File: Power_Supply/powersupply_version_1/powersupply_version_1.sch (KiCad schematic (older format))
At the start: 31 parts

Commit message: added to schematic
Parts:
- added C?: 100nF, symbol Device:C_Small
- added C? (x2): 12pF, symbol Device:C_Small
- added J?: Conn_01x05, symbol Connector_Generic:Conn_01x05
- added R?: 10k, symbol Device:R_Small_US
- added SW?: SW_Push, symbol Switch:SW_Push
- added U?: Atmega328P-AU, symbol powersupply_version_1:Atmega328P-AU
- added U?: TFT_LCD, symbol powersupply_version_1:TFT_LCD
- added Y?: Crystal, symbol Device:Crystal_Small
- R?: value R_Small_US -> 1k
- R?: value R_Small_US -> 5.13k
- R?: value R_Small_US -> 2.57k
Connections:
- net GND: now also U?.2 (VSS), C?.1, C?.2, C?.2, J?.5 (Pin_5), SW?.2, U?.2 (GND)
- net VCC: now reaches U?.3 (VDD)
- net VCC: now also C?.1, J?.4 (Pin_4), R?.2, SW?.1, U?.1 (VCC), U?.18 (AVCC), U?.4 (VCC), U?.6 (VCC), U?.8 (LED)
- net SDA: now reaches U?.4 (SDA)
- net SDA: now also U?.26 (PC3)
- net SCL: now reaches U?.5 (SCL)
- net SCL: now also U?.27 (PC4)
- new net: R?.1, U?.29 (PC6_(rst))
- new net: C?.2, U?.7 (PB6), Y?.2
- new net: C?.1, U?.8 (PB7), Y?.1
- new net CS: U?.3 (CS), U?.32 (PD2)
- new net DC: U?.1 (PD3), U?.5 (DC)
- new net MISO: J?.2 (Pin_2), U?.16 (PB4), U?.9 (MISO)
- new net MOSI: J?.3 (Pin_3), U?.15 (PB3), U?.6 (MOSI)
- new net Reset: U?.28 (PC5), U?.4 (reset)
- new net SCK: J?.1 (Pin_1), U?.17 (PB5), U?.7 (SCK)
- no-connect marks 4 -> 14

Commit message: pwr supply changes
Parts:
- removed C? (x12): C_Small, symbol Device:C_Small
- removed C?: 100nF, symbol Device:C_Small
- removed C? (x2): 12pF, symbol Device:C_Small
- removed D?: D_Zener, symbol Device:D_Zener_Small
- removed D?: D_Zener_Small, symbol Device:D_Zener_Small
- removed L?: L_Small, symbol Device:L_Small
- removed M? (x2): MNMOS, symbol pspice:MNMOS
- removed R? (x5): R_Small_US, symbol Device:R_Small_US
- removed R?: 10k, symbol Device:R_Small_US
- removed R?: R_small, symbol Device:R_Small_US
- removed R?: R_Small, symbol Device:R_Small_US
- removed R?: 1k, symbol Device:R_Small_US
- removed R?: 5.13k, symbol Device:R_Small_US
- removed U?: LM25118, symbol powersupply_version_1:LM25118
- removed U?: Atmega328P-AU, symbol powersupply_version_1:Atmega328P-AU
- removed Y?: Crystal, symbol Device:Crystal_Small
- added C? (x2): 0.1uF, symbol Device:C_Small
- added U?: ATSAMD10D14A-SS, Package_SO:SOIC-20W_7.5x12.8mm_P1.27mm, symbol MCU_Microchip_SAMD:ATSAMD10D14A-SS
- added U?: AP1117-15, Package_TO_SOT_SMD:SOT-223-3_TabPin2, symbol Regulator_Linear:AP1117-15
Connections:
- net labels added: +3.3V, GNDREF
- wire segments 111 -> 14
- no-connect marks 14 -> 11
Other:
- moved on the sheet: R?, U?

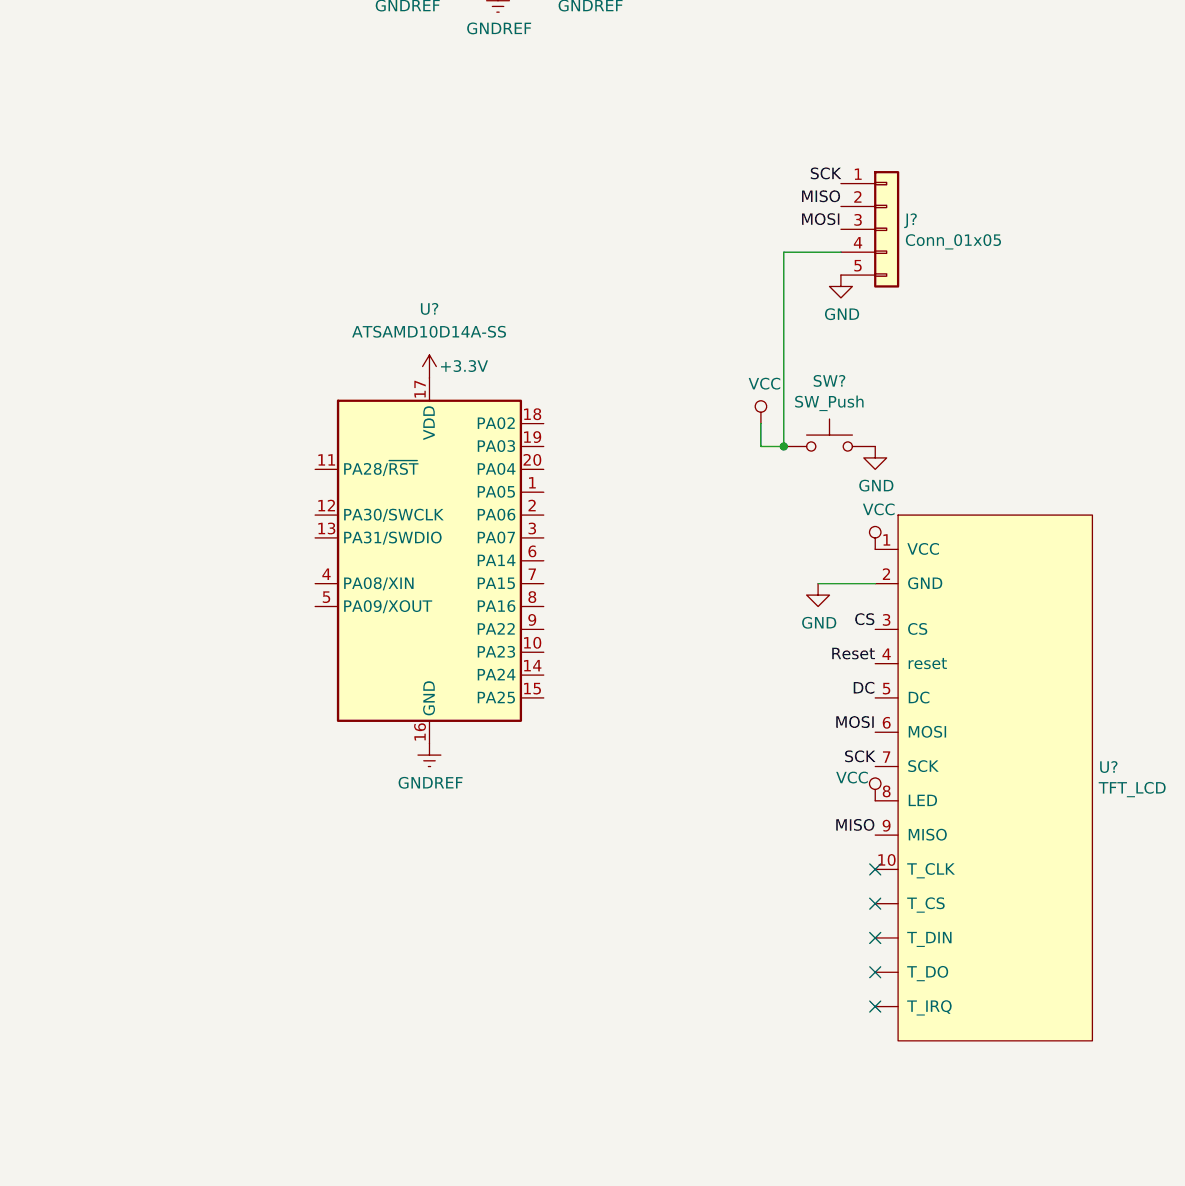
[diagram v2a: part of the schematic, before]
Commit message: removed op amp and sync connection
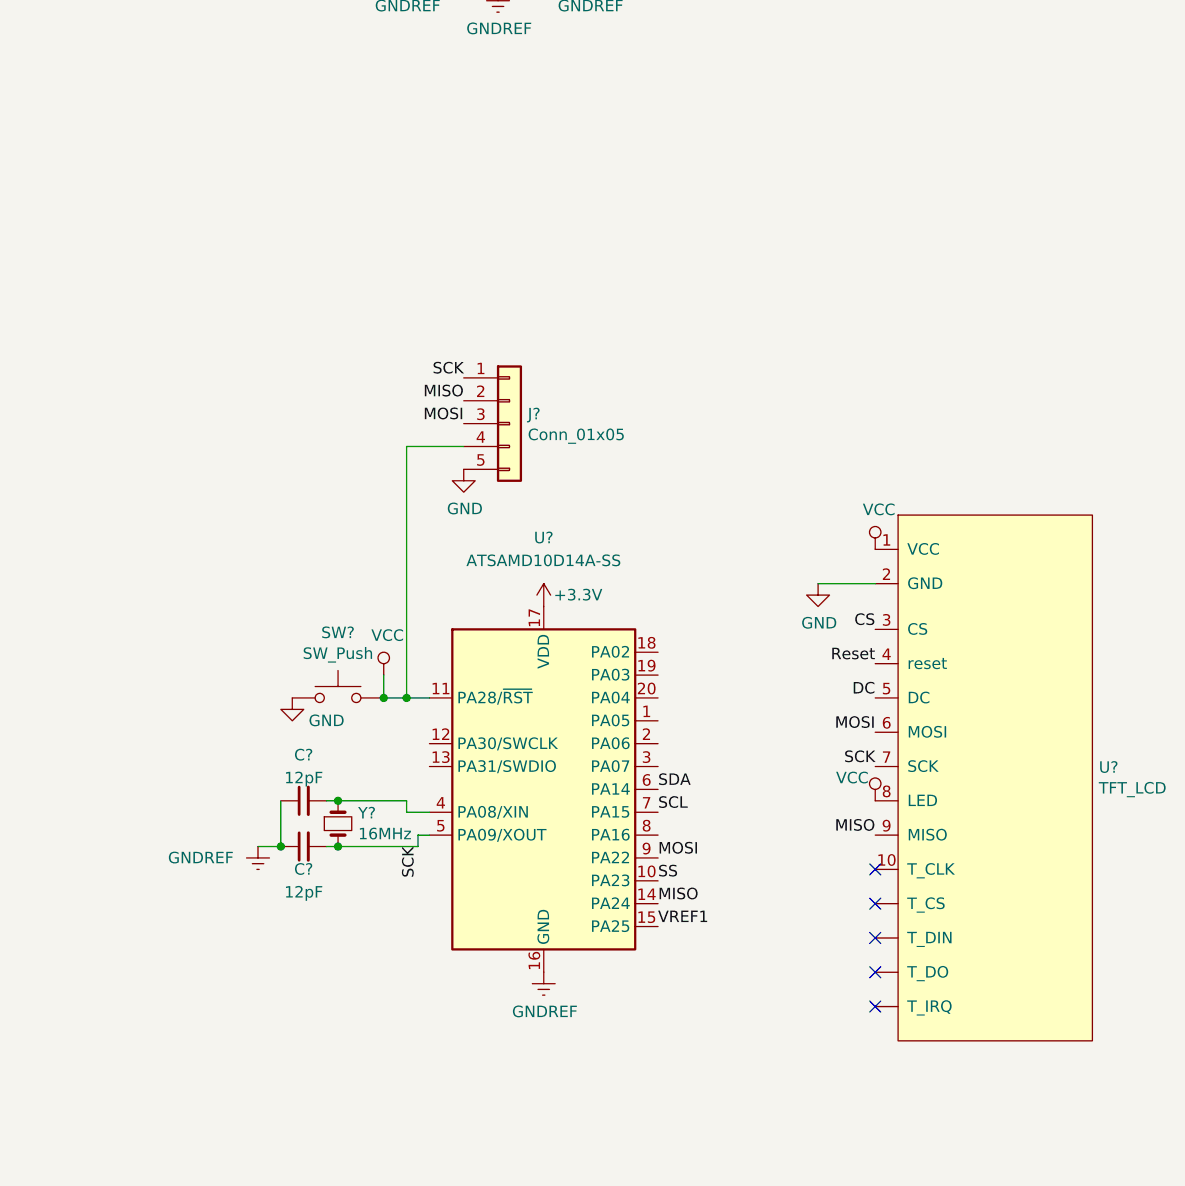
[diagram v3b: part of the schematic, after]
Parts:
- added C? (x2): 12pF, symbol Device:C_Small
- added Y?: 16MHz, symbol Device:Crystal_Small
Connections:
- net labels added: SS, VREF1
- wire segments 14 -> 25
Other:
- moved on the sheet: J?, SW?, U?
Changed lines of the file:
@@
-$Comp
-L power:VCC #PWR?
-U 1 1 5D3309E2
-P 3150 4900
-F 0 "#PWR?" H 3150 4750 50  0001 C CNN
-F 1 "VCC" H 3167 5073 50  0000 C CNN
-F 2 "" H 3150 4900 50  0001 C CNN
-F 3 "" H 3150 4900 50  0001 C CNN
-	1    3150 4900
-	1    0    0    -1
-$EndComp
-Wire Wire Line
-	3150 5000 3150 4900
-$Comp
-L Switch:SW_Push SW?
-U 1 1 5D3340CA
-P 3450 5000
-F 0 "SW?" H 3450 5285 50  0000 C CNN
-F 1 "SW_Push" H 3450 5194 50  0000 C CNN
-F 2 "" H 3450 5200 50  0001 C CNN
-F 3 "~" H 3450 5200 50  0001 C CNN
-	1    3450 5000
-	1    0    0    -1
-$EndComp
-$Comp
-L power:GND #PWR?
-U 1 1 5D335430
-P 3650 5000
-F 0 "#PWR?" H 3650 4750 50  0001 C CNN
-F 1 "GND" H 3655 4827 50  0000 C CNN
-F 2 "" H 3650 5000 50  0001 C CNN
-F 3 "" H 3650 5000 50  0001 C CNN
-	1    3650 5000
-	1    0    0    -1
-$EndComp
-Wire Wire Line
-	3150 5000 3250 5000
-Wire Wire Line
-	3250 5000 3250 4150
-Wire Wire Line
-	3250 4150 3500 4150
-Connection ~ 3250 5000
-$Comp
-L power:GND #PWR?
-U 1 1 5D33ECB0
-P 3500 4250
-F 0 "#PWR?" H 3500 4000 50  0001 C CNN
-F 1 "GND" H 3505 4077 50  0000 C CNN
-F 2 "" H 3500 4250 50  0001 C CNN
-F 3 "" H 3500 4250 50  0001 C CNN
-	1    3500 4250
-	1    0    0    -1
-$EndComp
-$Comp
-L Connector_Generic:Conn_01x05 J?
-U 1 1 5D3457C6
-P 3700 4050
-F 0 "J?" H 3780 4092 50  0000 L CNN
-F 1 "Conn_01x05" H 3780 4001 50  0000 L CNN
-F 2 "" H 3700 4050 50  0001 C CNN
-F 3 "~" H 3700 4050 50  0001 C CNN
-	1    3700 4050
-	1    0    0    -1
-$EndComp
-Text Label 3500 4050 2    50   ~ 0
-MOSI
-Text Label 3500 3950 2    50   ~ 0
-MISO
-Text Label 3500 3850 2    50   ~ 0
-SCK
 $Comp
 L power:VCC #PWR?
@@
 L MCU_Microchip_SAMD:ATSAMD10D14A-SS U?
 U 1 1 5D3D0FF3
-P 1700 5500
-F 0 "U?" H 1700 6600 50  0000 C CNN
-F 1 "ATSAMD10D14A-SS" H 1700 6500 50  0000 C CNN
-F 2 "Package_SO:SOIC-20W_7.5x12.8mm_P1.27mm" H 1700 4350 50  0001 C CNN
-F 3 "http://ww1.microchip.com/downloads/en/DeviceDoc/Atmel-42242-SAM-D10_Datasheet.pdf" H 1700 4600 50  0001 C CNN
-	1    1700 5500
+P 2200 6500
+F 0 "U?" H 2200 7600 50  0000 C CNN
+F 1 "ATSAMD10D14A-SS" H 2200 7500 50  0000 C CNN
+F 2 "Package_SO:SOIC-20W_7.5x12.8mm_P1.27mm" H 2200 5350 50  0001 C CNN
+F 3 "http://ww1.microchip.com/downloads/en/DeviceDoc/Atmel-42242-SAM-D10_Datasheet.pdf" H 2200 5600 50  0001 C CNN
+	1    2200 6500
 	1    0    0    -1
 $EndComp
@@
 L power:GNDREF #PWR?
 U 1 1 5D3FD3BC
-P 1700 6300
-F 0 "#PWR?" H 1700 6050 50  0001 C CNN
-F 1 "GNDREF" H 1705 6127 50  0000 C CNN
-F 2 "" H 1700 6300 50  0001 C CNN
-F 3 "" H 1700 6300 50  0001 C CNN
-	1    1700 6300
+P 2200 7300
+F 0 "#PWR?" H 2200 7050 50  0001 C CNN
+F 1 "GNDREF" H 2205 7127 50  0000 C CNN
+F 2 "" H 2200 7300 50  0001 C CNN
+F 3 "" H 2200 7300 50  0001 C CNN
+	1    2200 7300
 	1    0    0    -1
 $EndComp
@@
 L power:+3.3V #PWR?
 U 1 1 5D3FE02C
-P 1700 4700
-F 0 "#PWR?" H 1700 4550 50  0001 C CNN
-F 1 "+3.3V" H 1850 4750 50  0000 C CNN
-F 2 "" H 1700 4700 50  0001 C CNN
-F 3 "" H 1700 4700 50  0001 C CNN
-	1    1700 4700
-	1    0    0    -1
-$EndComp
+P 2200 5700
+F 0 "#PWR?" H 2200 5550 50  0001 C CNN
+F 1 "+3.3V" H 2350 5750 50  0000 C CNN
+F 2 "" H 2200 5700 50  0001 C CNN
+F 3 "" H 2200 5700 50  0001 C CNN
+	1    2200 5700
+	1    0    0    -1
+$EndComp
+Text Label 1850 4700 2    50   ~ 0
+SCK
+Text Label 1850 4800 2    50   ~ 0
+MISO
+Text Label 1850 4900 2    50   ~ 0
+MOSI
+$Comp
+L Connector_Generic:Conn_01x05 J?
+U 1 1 5D3457C6
+P 2050 4900
+F 0 "J?" H 2130 4942 50  0000 L CNN
+F 1 "Conn_01x05" H 2130 4851 50  0000 L CNN
+F 2 "" H 2050 4900 50  0001 C CNN
+F 3 "~" H 2050 4900 50  0001 C CNN
+	1    2050 4900
+	1    0    0    -1
+$EndComp
+$Comp
+L power:GND #PWR?
+U 1 1 5D33ECB0
+P 1850 5100
+F 0 "#PWR?" H 1850 4850 50  0001 C CNN
+F 1 "GND" H 1855 4927 50  0000 C CNN
+F 2 "" H 1850 5100 50  0001 C CNN
+F 3 "" H 1850 5100 50  0001 C CNN
+	1    1850 5100
+	1    0    0    -1
+$EndComp
+Wire Wire Line
+	1600 5000 1850 5000
+$Comp
+L power:VCC #PWR?
+U 1 1 5D3309E2
+P 1500 6000
+F 0 "#PWR?" H 1500 5850 50  0001 C CNN
+F 1 "VCC" H 1517 6173 50  0000 C CNN
+F 2 "" H 1500 6000 50  0001 C CNN
+F 3 "" H 1500 6000 50  0001 C CNN
+	1    1500 6000
+	1    0    0    -1
+$EndComp
+Wire Wire Line
+	1500 6100 1500 6000
+$Comp
+L Switch:SW_Push SW?
+U 1 1 5D3340CA
+P 1300 6100
+F 0 "SW?" H 1300 6385 50  0000 C CNN
+F 1 "SW_Push" H 1300 6294 50  0000 C CNN
+F 2 "" H 1300 6300 50  0001 C CNN
+F 3 "~" H 1300 6300 50  0001 C CNN
+	1    1300 6100
+	1    0    0    -1
+$EndComp
+$Comp
+L power:GND #PWR?
+U 1 1 5D335430
+P 1100 6100
+F 0 "#PWR?" H 1100 5850 50  0001 C CNN
+F 1 "GND" H 1250 6000 50  0000 C CNN
+F 2 "" H 1100 6100 50  0001 C CNN
+F 3 "" H 1100 6100 50  0001 C CNN
+	1    1100 6100
+	1    0    0    -1
+$EndComp
+Wire Wire Line
+	1600 5000 1600 6100
+Wire Wire Line
+	1700 6100 1600 6100
+Connection ~ 1500 6100
+Connection ~ 1600 6100
+Wire Wire Line
+	1600 6100 1500 6100
+$Comp
+L Device:Crystal_Small Y?
+U 1 1 5D41A5D2
+P 1300 6650
+F 0 "Y?" V 1254 6738 50  0000 L CNN
+F 1 "16MHz" V 1345 6738 50  0000 L CNN
+F 2 "" H 1300 6650 50  0001 C CNN
+F 3 "~" H 1300 6650 50  0001 C CNN
+	1    1300 6650
+	0    1    1    0
+$EndComp
+$Comp
+L Device:C_Small C?
+U 1 1 5D41D67B
+P 1150 6550
+F 0 "C?" V 1350 6550 50  0000 C CNN
+F 1 "12pF" V 1250 6550 50  0000 C CNN
+F 2 "" H 1150 6550 50  0001 C CNN
+F 3 "~" H 1150 6550 50  0001 C CNN
+	1    1150 6550
+	0    -1   -1   0
+$EndComp
+$Comp
+L Device:C_Small C?
+U 1 1 5D41F47A
+P 1150 6750
+F 0 "C?" V 1050 6750 50  0000 C CNN
+F 1 "12pF" V 950 6750 50  0000 C CNN
+F 2 "" H 1150 6750 50  0001 C CNN
+F 3 "~" H 1150 6750 50  0001 C CNN
+	1    1150 6750
+	0    -1   -1   0
+$EndComp
+Wire Wire Line
+	1700 6600 1600 6600
+Wire Wire Line
+	1600 6600 1600 6550
+Wire Wire Line
+	1600 6550 1300 6550
+Wire Wire Line
+	1250 6550 1300 6550
+Connection ~ 1300 6550
+Wire Wire Line
+	1300 6750 1650 6750
+Wire Wire Line
+	1650 6750 1650 6700
+Wire Wire Line
+	1650 6700 1700 6700
+$Comp
+L power:GNDREF #PWR?
+U 1 1 5D42290E
+P 950 6750
+F 0 "#PWR?" H 950 6500 50  0001 C CNN
+F 1 "GNDREF" H 700 6700 50  0000 C CNN
+F 2 "" H 950 6750 50  0001 C CNN
+F 3 "" H 950 6750 50  0001 C CNN
+	1    950  6750
+	1    0    0    -1
+$EndComp
+Wire Wire Line
+	1050 6550 1050 6750
+Wire Wire Line
+	1250 6750 1300 6750
+Connection ~ 1300 6750
+Wire Wire Line
+	950  6750 1050 6750
+Connection ~ 1050 6750
+Text Label 2700 6800 0    50   ~ 0
+MOSI
+Text Label 2700 7000 0    50   ~ 0
+MISO
+Text Label 2700 6500 0    50   ~ 0
+SDA
+Text Label 2700 6600 0    50   ~ 0
+SCL
+Text Label 1650 6750 3    50   ~ 0
+SCK
+Text Label 2700 6900 0    50   ~ 0
+SS
+Text Label 2700 7100 0    50   ~ 0
+VREF1
 $EndSCHEMATC
